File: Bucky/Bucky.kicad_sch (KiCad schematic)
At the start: 28 parts, among them J1 XT60PW-M, J10 XT30AW-M, J11 XT30AW-M, J12 XT30AW-M, J13 XT30AW-M, J14 XT30AW-M, J2 XT60PW-M, J3 XT30PW-M, J4 XT30PW-M, J5 XT30PW-M, J6 XT30PW-M, J7 XT30AW-M, J8 XT30AW-M, J9 XT30AW-M

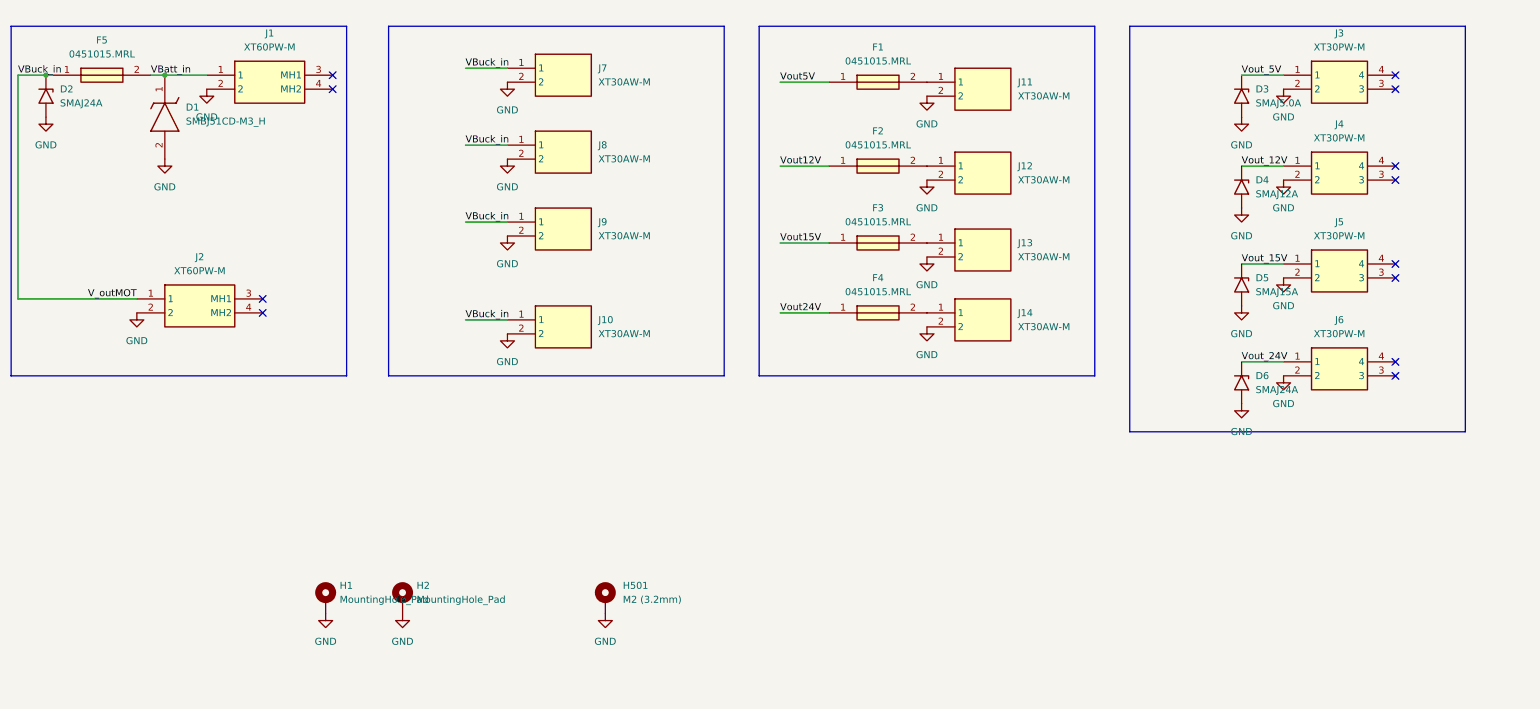
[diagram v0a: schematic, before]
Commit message: fixed xt60 polarity connection
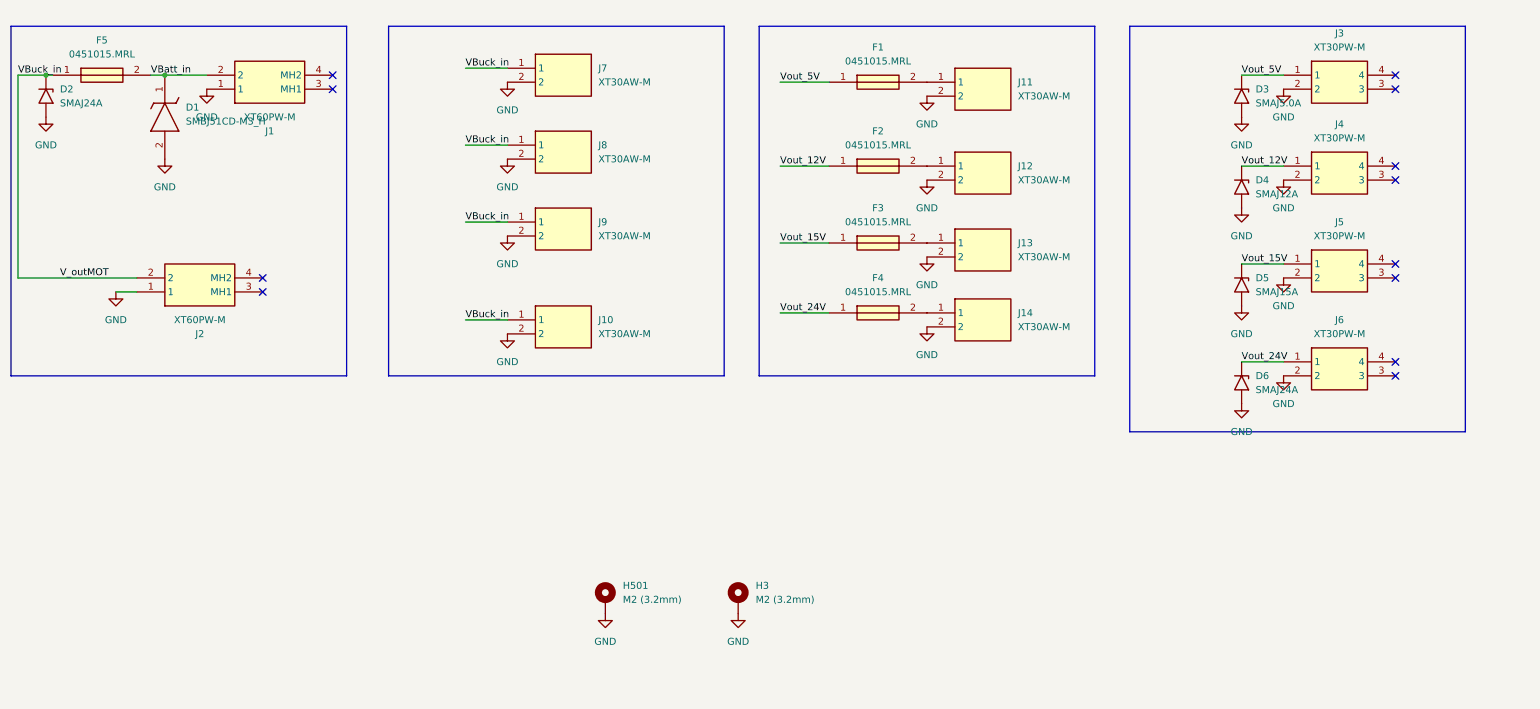
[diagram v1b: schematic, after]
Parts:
- removed H1, H2: MountingHole_Pad, symbol Mechanical:MountingHole_Pad
- added H3: M2 (3.2mm), MountingHole:MountingHole_2.2mm_M2_Pad_Via, symbol Mechanical:MountingHole_Pad
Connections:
- net Vout12V is gone; now on net Vout_12V: F2.1
- net Vout15V is gone; now on net Vout_15V: F3.1
- net Vout24V is gone; now on net Vout_24V: F4.1
- net Vout5V is gone; now on net Vout_5V: F1.1
- net GND: now also J1.1, J2.1, H3.1; no longer J1.2, J2.2
- net VBatt_in: now also J1.2; no longer J1.1
- net VBuck_in: now also J2.2; no longer J2.1
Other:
- moved on the sheet: J2

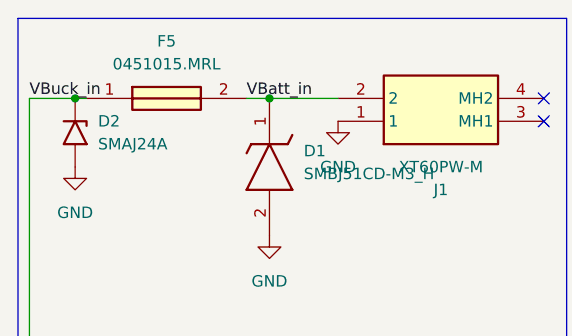
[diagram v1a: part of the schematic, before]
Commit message: spaced vertical connectors, added 40A fuse
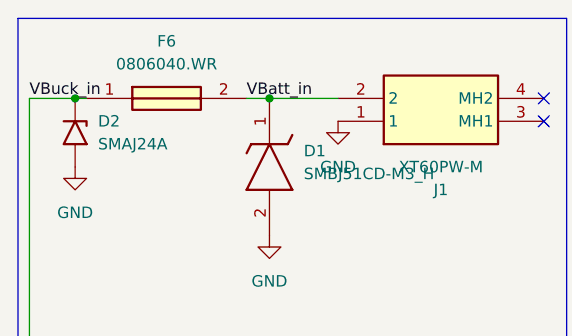
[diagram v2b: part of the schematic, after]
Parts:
- removed F5: 0451015.MRL, FUSC6127X294N, symbol SamacSys_Parts:0451015.MRL
- added F6: 0806040.WR, FUSC3216X110N, symbol SamacSys_Parts:0806040.WR
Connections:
- net VBatt_in: now also F6.2
- net VBuck_in: now also F6.1

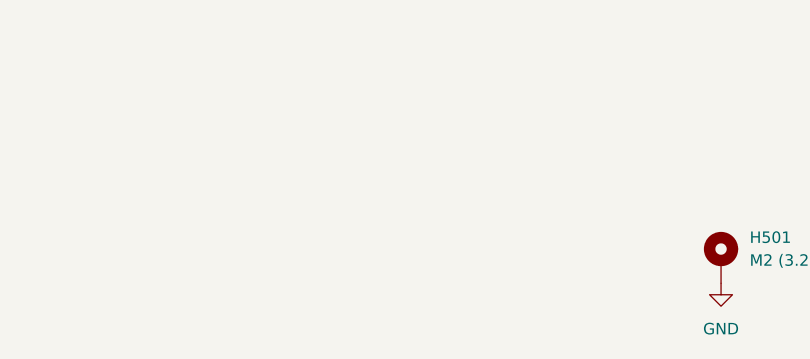
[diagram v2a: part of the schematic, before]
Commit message: added 4 screws, switched motout and batt in
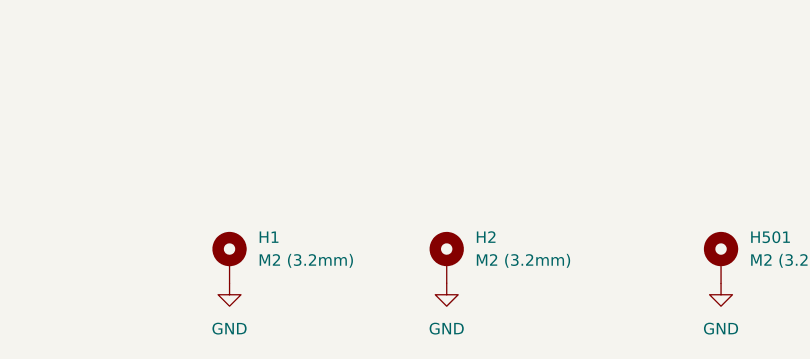
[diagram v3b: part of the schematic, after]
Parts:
- added H1, H2: M2 (3.2mm), MountingHole:MountingHole_2.2mm_M2_Pad_Via, symbol Mechanical:MountingHole_Pad
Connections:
- net GND: now also H1.1, H2.1

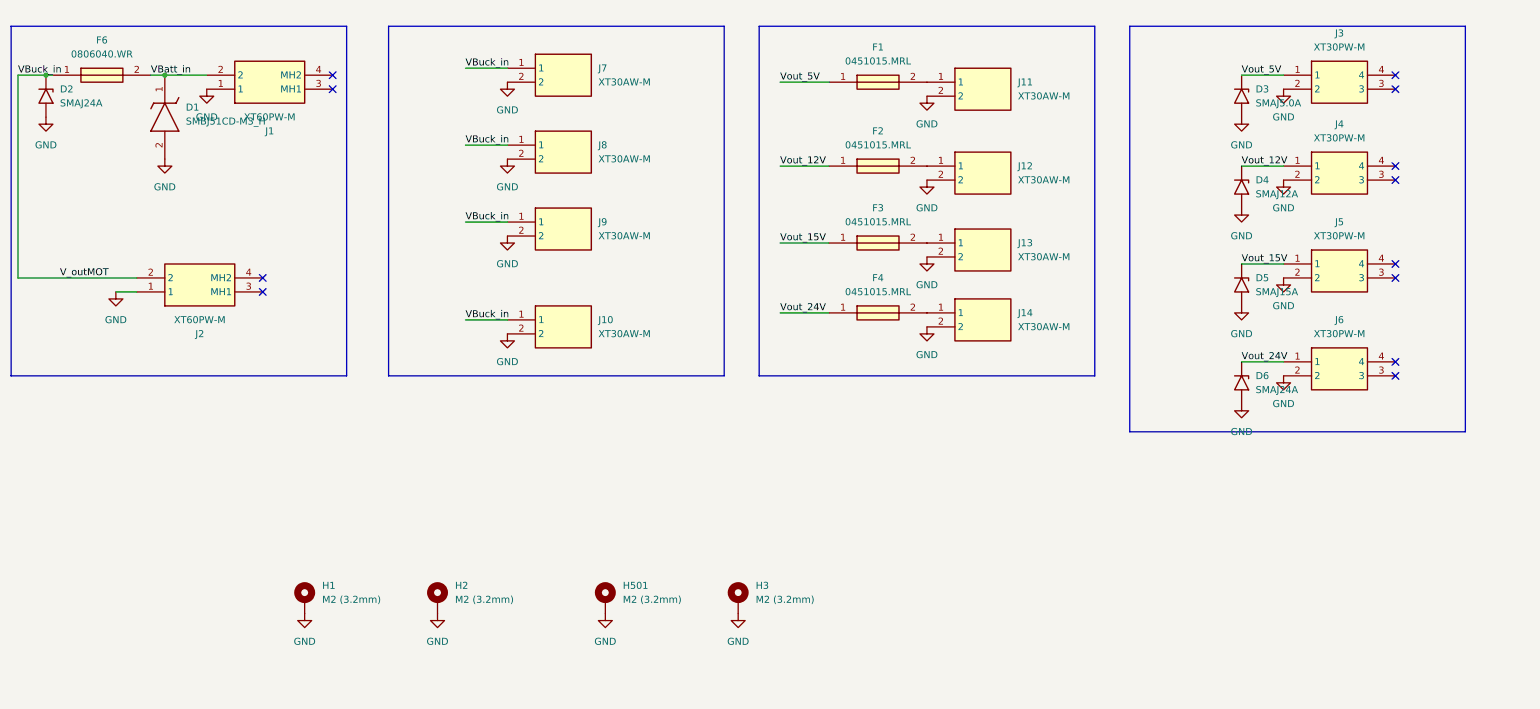
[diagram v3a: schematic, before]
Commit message: added features from GEODE to the schematics
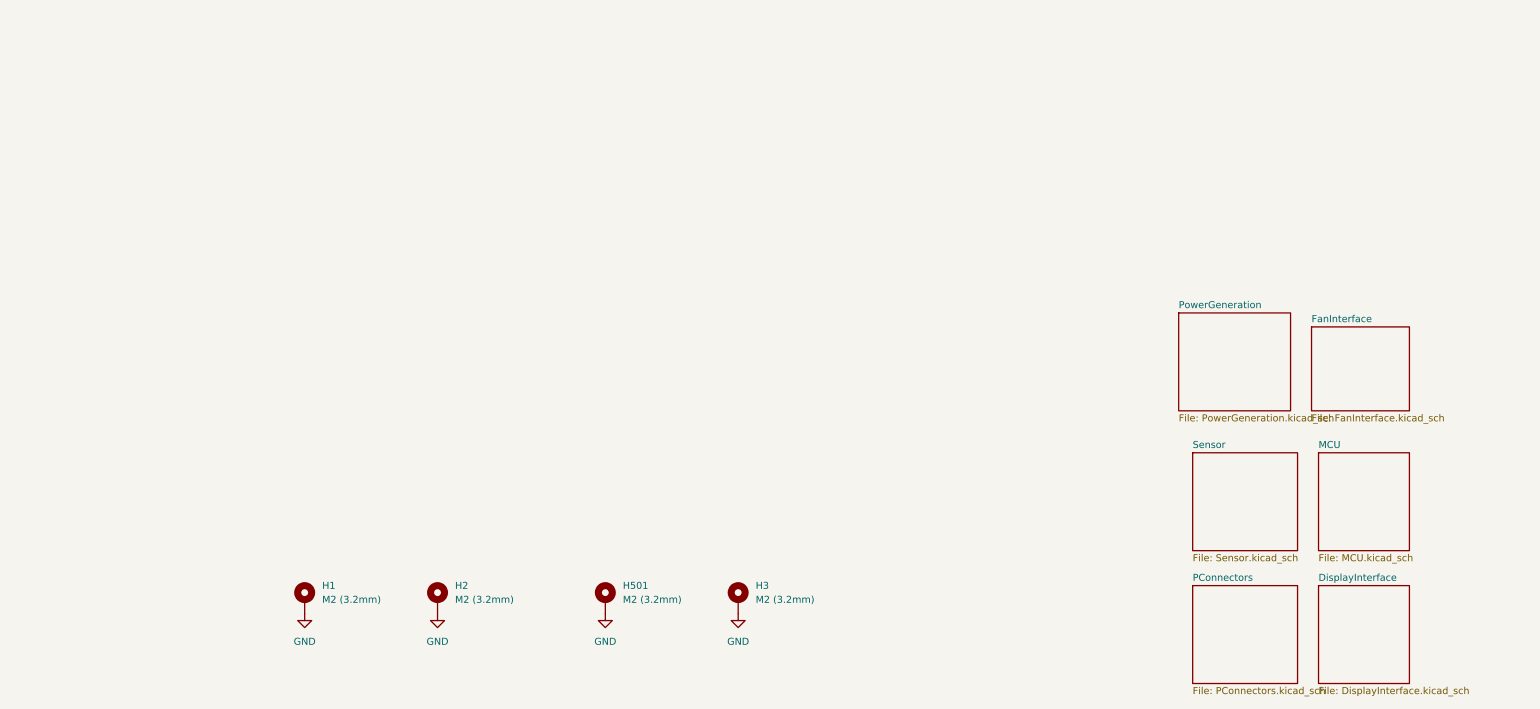
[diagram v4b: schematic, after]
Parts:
- removed D1: SMBJ51CD-M3_H, DIOM5436X244N, symbol SamacSys_Parts:SMBJ51CD-M3_H
- removed D2, D6: SMAJ24A, Diode_SMD:D_SMA, symbol Diode:SMAJ24A
- removed D3: SMAJ5.0A, Diode_SMD:D_SMA, symbol Diode:SMAJ5.0A
- removed D4: SMAJ12A, Diode_SMD:D_SMA, symbol Diode:SMAJ12A
- removed D5: SMAJ15A, Diode_SMD:D_SMA, symbol Diode:SMAJ15A
- removed F1, F2, F3, F4: 0451015.MRL, FUSC6127X294N, symbol SamacSys_Parts:0451015.MRL
- removed F6: 0806040.WR, FUSC3216X110N, symbol SamacSys_Parts:0806040.WR
- removed J1, J2: XT60PW-M, XT60PWM, symbol SamacSys_Parts:XT60PW-M
- removed J10, J11, J12, J13, J14, J7, J8, J9: XT30AW-M, XT30AWM, symbol SamacSys_Parts:XT30AW-M
- removed J3, J4, J5, J6: XT30PW-M, XT30PWM, symbol SamacSys_Parts:XT30PW-M
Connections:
- no-connect marks 12 -> 0
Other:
- added sheet DisplayInterface (DisplayInterface.kicad_sch)
- added sheet FanInterface (FanInterface.kicad_sch)
- added sheet MCU (MCU.kicad_sch)
- added sheet PConnectors (PConnectors.kicad_sch)
- added sheet PowerGeneration (PowerGeneration.kicad_sch)
- added sheet Sensor (Sensor.kicad_sch)

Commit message: adapted schematics and added more protection from GEODE (Reverse Current)
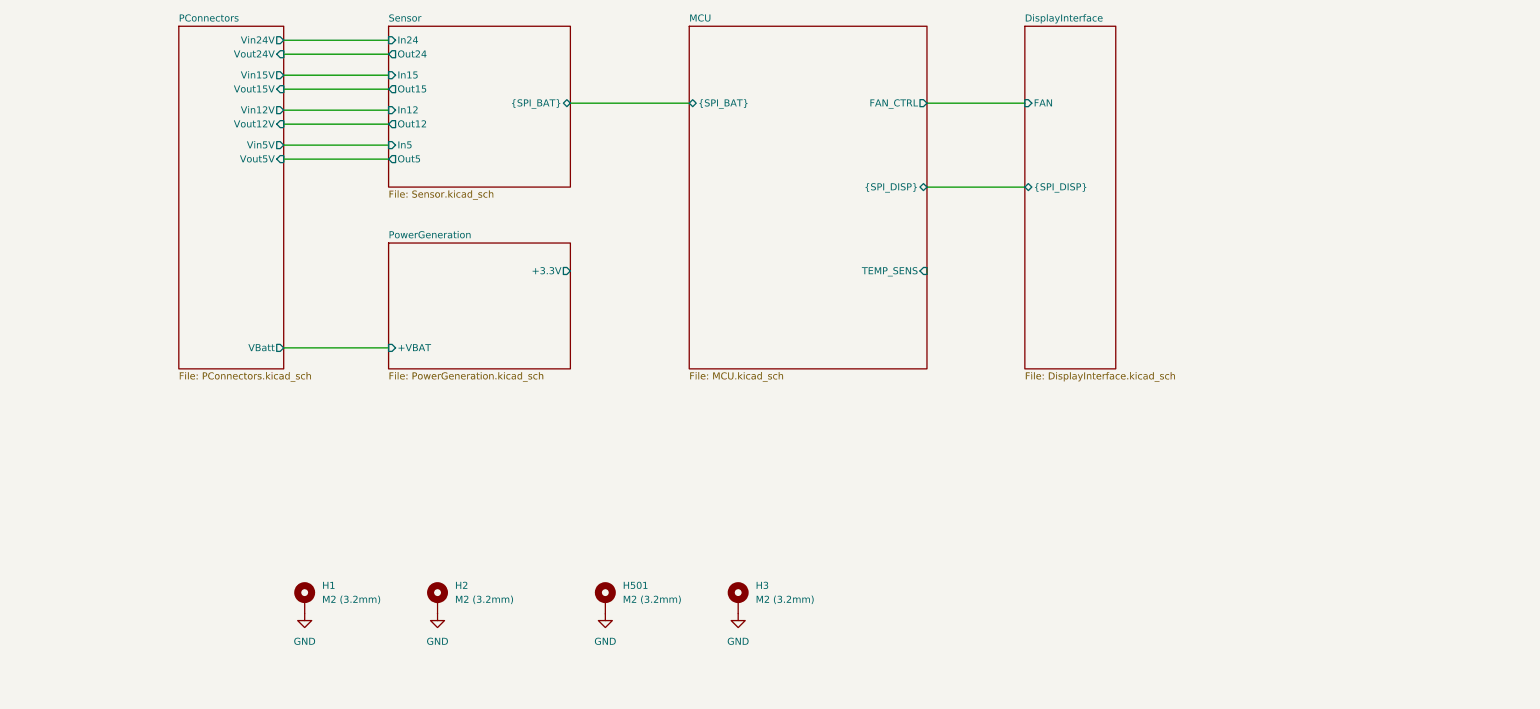
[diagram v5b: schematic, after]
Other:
- removed sheet FanInterface
- sheet DisplayInterface ports: added FAN, {SPI_DISP}; removed none
- sheet MCU ports: added FAN_CTRL, TEMP_SENS, {SPI_BAT}, {SPI_DISP}; removed none
- sheet PConnectors ports: added VBatt, Vin12V, Vin15V, Vin24V, Vin5V, Vout12V, Vout15V, Vout24V, Vout5V; removed none
- sheet PowerGeneration ports: added +3.3V, +VBAT; removed none
- sheet Sensor ports: added In12, In15, In24, In5, Out12, Out15, Out24, Out5, {SPI_BAT}; removed none

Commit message: upadated scchematics
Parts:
- added C10, C11, C12, C9: 1u X7R 10V, 0_capacitor_smd:C_0402_1005_DensityHigh, symbol Device:C
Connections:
- net GND: now also C10.2, C11.2, C12.2, C9.2; no longer H1.1, H2.1, H3.1, H501.1
- new net: C10.1, H2.1
- new net: C12.1, H3.1
- new net: C11.1, H501.1
- new net: C9.1, H1.1
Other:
- removed sheet DisplayInterface
- sheet MCU ports: added none; removed FAN_CTRL, TEMP_SENS, {SPI_DISP}
- sheet PConnectors ports: added V_Batt; removed none
- sheet Sensor ports: added InBatt, OutBatt; removed none

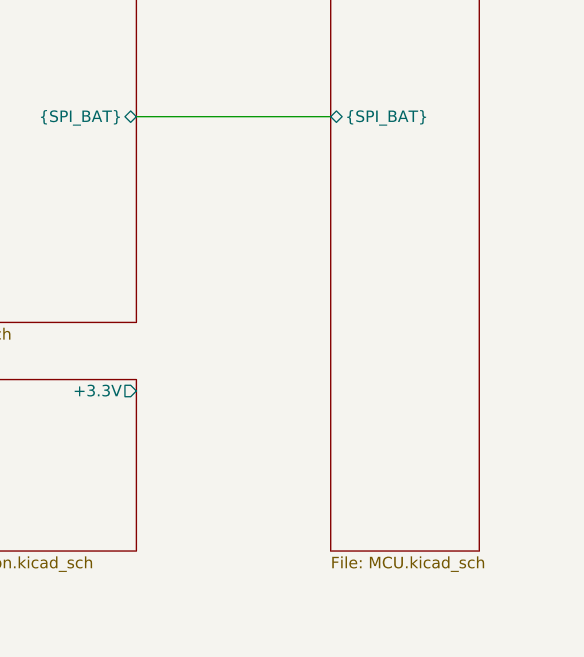
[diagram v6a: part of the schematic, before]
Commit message: created Bucky++ with new template and e-fuses
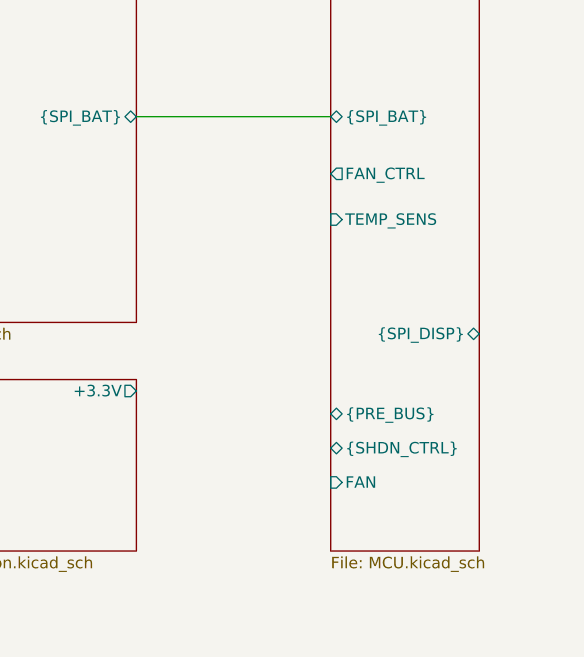
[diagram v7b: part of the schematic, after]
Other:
- sheet MCU ports: added FAN, FAN_CTRL, TEMP_SENS, {PRE_BUS}, {SHDN_CTRL}, {SPI_DISP}; removed none
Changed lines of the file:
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@@
+			)
+		)
+		(pin "FAN_CTRL" output
+			(at 138.43 55.88 180)
+			(effects
+				(font
+					(size 1.27 1.27)
+				)
+				(justify left)
+			)
+		)
+		(pin "{SHDN_CTRL}" bidirectional
+			(at 138.43 86.36 180)
+			(effects
+				(font
+					(size 1.27 1.27)
+				)
+				(justify left)
+			)
+		)
+		(pin "{SPI_DISP}" bidirectional
+			(at 154.94 73.66 0)
+			(effects
+				(font
+					(size 1.27 1.27)
+				)
+				(justify right)
+			)
+		)
+		(pin "{PRE_BUS}" bidirectional
+			(at 138.43 82.55 180)
+			(effects
+				(font
+					(size 1.27 1.27)
+				)
+				(justify left)
+			)
+		)
+		(pin "FAN" input
+			(at 138.43 90.17 180)
+			(effects
+				(font
+					(size 1.27 1.27)
+				)
+				(justify left)
+			)
+		)
+		(pin "TEMP_SENS" input
+			(at 138.43 60.96 180)
+			(effects
+				(font
+					(size 1.27 1.27)
+				)
+				(justify left)
 			)
 		)
